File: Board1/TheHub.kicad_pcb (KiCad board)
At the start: 2 copper layers, 118.7 x 184.1 mm, 51 parts, among them J11 RFD900, J12 I2C_1 Test Point, J13 I2C_2 Test Point, J15 GPIO Test, J16 I2C_3 Test Point, J17 12V OUT, J23 NucleoRight, J5 NucleoLeft, J8 12V MAIN POWER, U10 ADXL377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

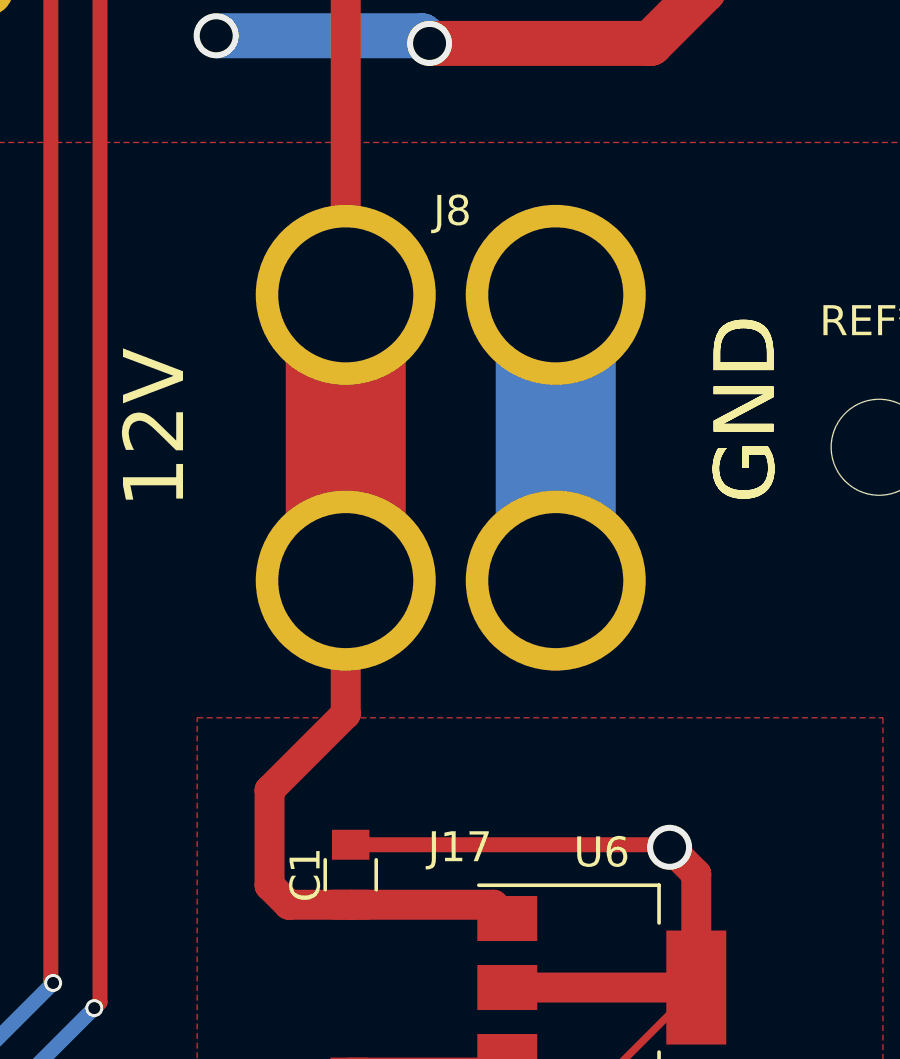
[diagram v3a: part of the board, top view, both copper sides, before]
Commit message: Update XT60 connectors, replae old XT60 footprint on board, generate new gerbers
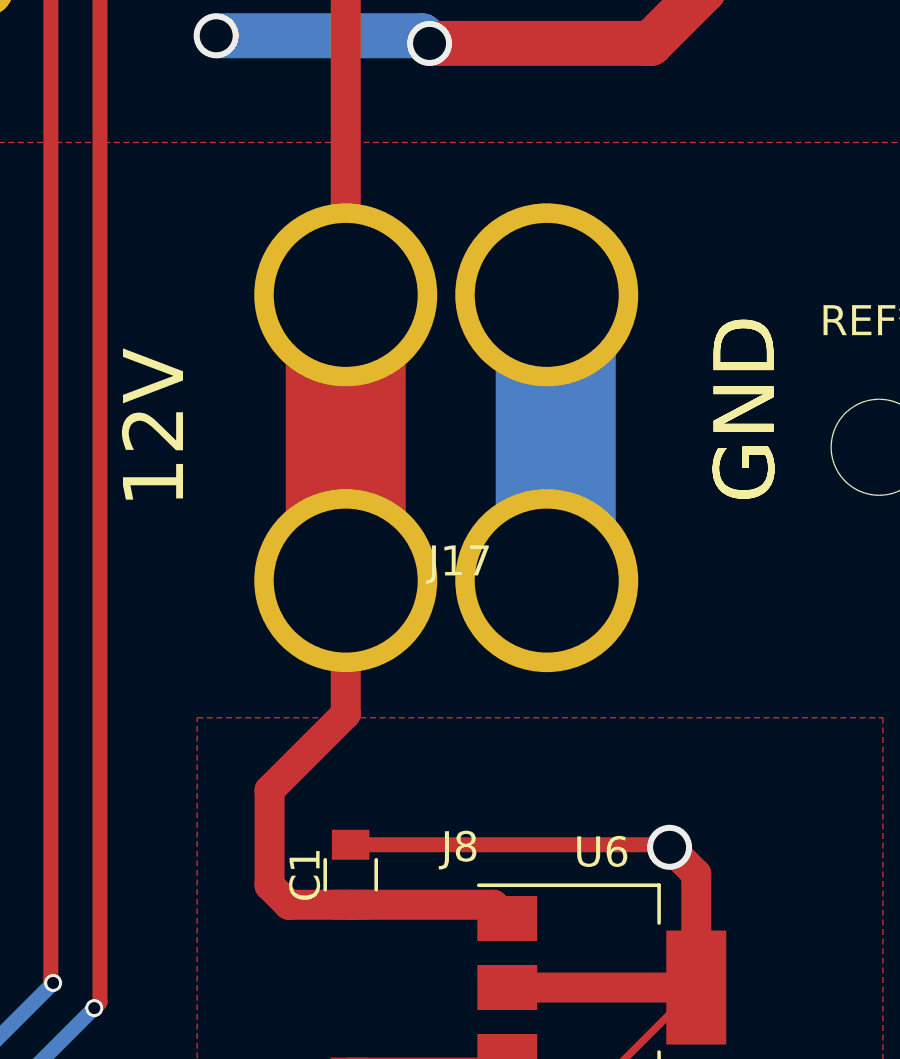
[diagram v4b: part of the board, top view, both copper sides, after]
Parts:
- moved J17 9.53 mm to (158.8, 87.6)
- moved J8 9.53 mm to (158.8, 97.2)
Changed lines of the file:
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@@
   )
   (setup
-    (last_trace_width 1)
+    (last_trace_width 0.25)
     (user_trace_width 0.5)
     (user_trace_width 1)
@@
     )
   )
-  (module FoxWestern:XT60 (layer F.Cu)
-    (at 158.75 97.155)
-    (fp_text reference J17 (at 3.81 8.89) (layer F.SilkS)
-      (effects (font (size 1 1) (thickness 0.15)))
-    )
-    (fp_text value "12V OUT" (at 1.27 -7.62) (layer F.Fab)
-      (effects (font (size 1 1) (thickness 0.15)))
-    )
-    (pad 1 thru_hole circle (at 0 0) (size 6 6) (drill 4.5) (layers *.Cu *.Mask)
-      (net 1 +12V))
-    (pad 2 thru_hole circle (at 7 0) (size 6 6) (drill 4.5) (layers *.Cu *.Mask)
-      (net 2 GND))
-  )
   (module Pin_Headers:Pin_Header_Straight_1x03_Pitch2.54mm (layer F.Cu)
     (at 167.767 173.482 180)
@@
       (rotate (xyz 0 0 90))
     )
-  )
-  (module FoxWestern:XT60 (layer F.Cu)
-    (at 158.75 87.63)
-    (fp_text reference J8 (at 3.556 -2.794) (layer F.SilkS)
-      (effects (font (size 1 1) (thickness 0.15)))
-    )
-    (fp_text value "12V MAIN POWER" (at 1.27 -7.62) (layer F.Fab)
-      (effects (font (size 1 1) (thickness 0.15)))
-    )
-    (pad 1 thru_hole circle (at 0 0) (size 6 6) (drill 4.5) (layers *.Cu *.Mask)
-      (net 1 +12V))
-    (pad 2 thru_hole circle (at 7 0) (size 6 6) (drill 4.5) (layers *.Cu *.Mask)
-      (net 2 GND))
   )
   (module LEDs:LED_0805 (layer F.Cu)
@@
       (xy -15.895129 12.091526) (xy -15.76892 12.11999) (xy -15.549608 12.131504) (xy -15.333323 12.096166)) (layer B.SilkS) (width 0.01))
   )
+  (module FoxWestern:XT60 (layer F.Cu)
+    (at 158.75 97.155)
+    (fp_text reference J8 (at 3.81 8.89) (layer F.SilkS)
+      (effects (font (size 1 1) (thickness 0.15)))
+    )
+    (fp_text value "12V MAIN POWER" (at 1.27 -7.62) (layer F.Fab)
+      (effects (font (size 1 1) (thickness 0.15)))
+    )
+    (pad 1 thru_hole circle (at 0 0) (size 6.1 6.1) (drill 4.8) (layers *.Cu *.Mask)
+      (net 1 +12V))
+    (pad 2 thru_hole circle (at 6.7 0) (size 6.1 6.1) (drill 4.8) (layers *.Cu *.Mask)
+      (net 2 GND))
+  )
+  (module FoxWestern:XT60 (layer F.Cu)
+    (at 158.75 87.63)
+    (fp_text reference J17 (at 3.81 8.89) (layer F.SilkS)
+      (effects (font (size 1 1) (thickness 0.15)))
+    )
+    (fp_text value "12V OUT" (at 1.27 -7.62) (layer F.Fab)
+      (effects (font (size 1 1) (thickness 0.15)))
+    )
+    (pad 1 thru_hole circle (at 0 0) (size 6.1 6.1) (drill 4.8) (layers *.Cu *.Mask)
+      (net 1 +12V))
+    (pad 2 thru_hole circle (at 6.7 0) (size 6.1 6.1) (drill 4.8) (layers *.Cu *.Mask)
+      (net 2 GND))
+  )
   (gr_text GND (at 164.465 168.275) (layer F.SilkS)
